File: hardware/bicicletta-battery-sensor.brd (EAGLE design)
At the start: 45.7 x 19.1 mm, 15 parts, among them IC1 LMP92064, IC2 TXB0108

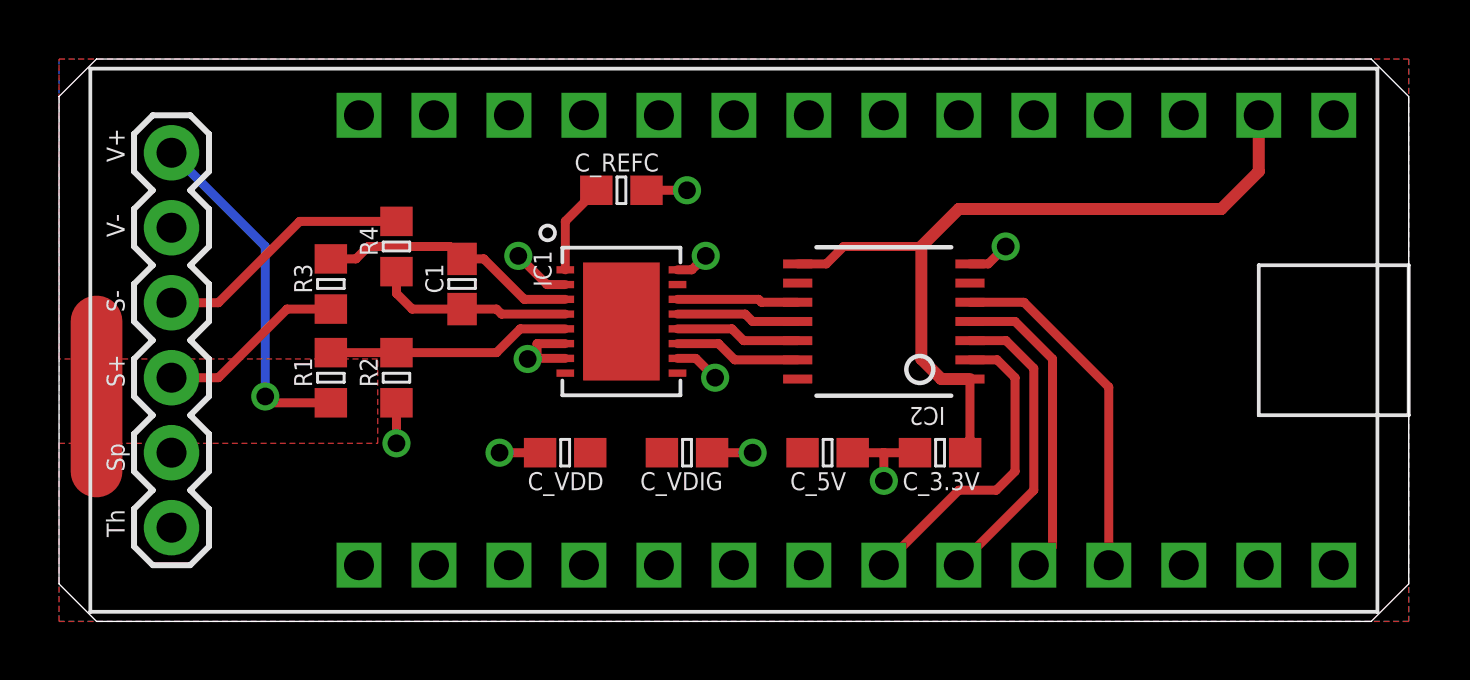
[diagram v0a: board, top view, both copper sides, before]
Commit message: Trying out a new level shifter, as the previous integrated one proved awfully fiddly in practice.
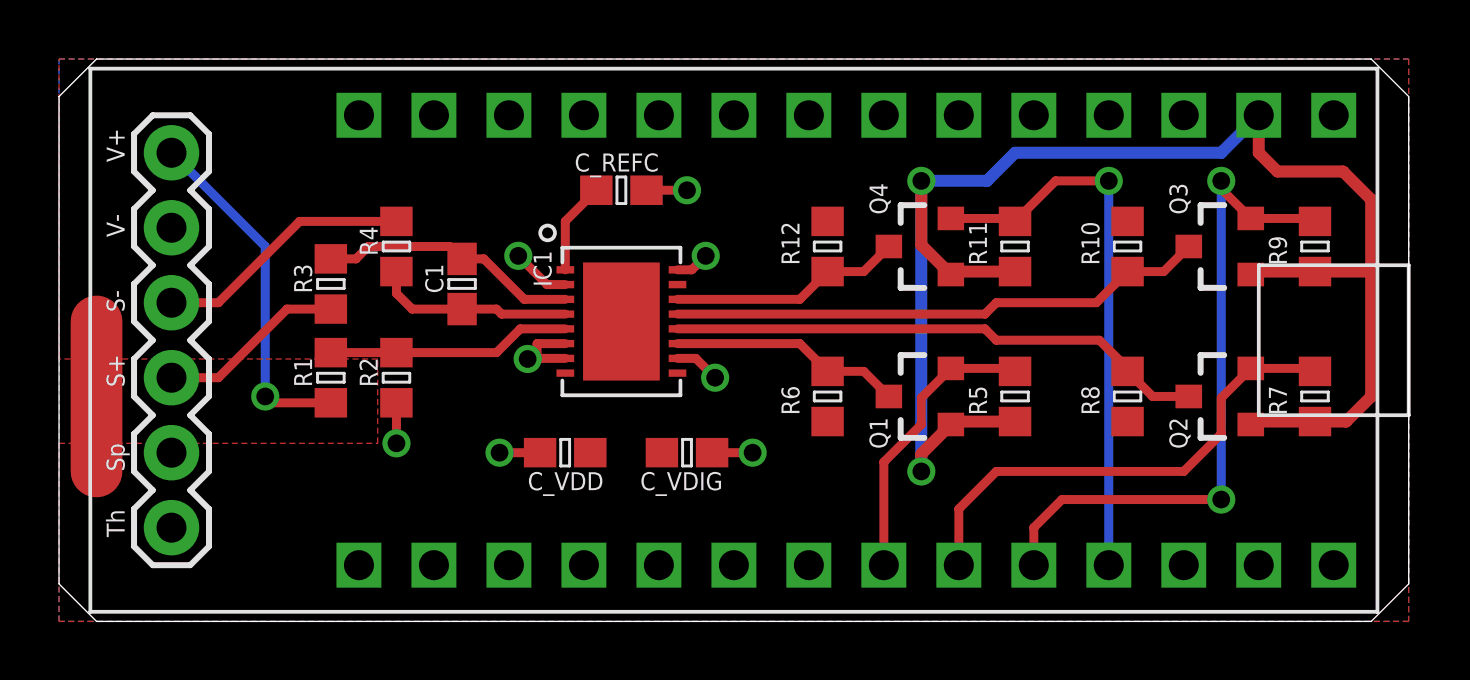
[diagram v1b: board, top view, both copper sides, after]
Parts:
- removed C_3.3V, C_5V: 0.1uF, rcl:C0603
- removed IC2: TXB0108, adafruit:TSSOP14
- added Q1, Q2, Q3, Q4: BSS138, SparkFun-DiscreteSemi:SOT23-3
- added R10, R11, R12, R5, R6, R7, R8, R9: 10K, rcl:R0603
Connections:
- net 3.3V: now also Q1.1, Q2.1, Q3.1, Q4.1, R11.2, R5.2, R7.2, R9.2; no longer C_3.3V.1, IC2.1, IC2.8
- net 5V: now also R10.2, R12.2, R6.2, R8.2; no longer C_5V.1, IC2.14
- net CLK: now also Q3.2, R9.1; no longer IC2.4
- net CLK_5: now also Q3.3, R10.1; no longer IC2.11
- net GND: no longer C_3.3V.2, C_5V.2, IC2.7
- net MISO: now also Q1.2, R5.1; no longer IC2.2
- net MISO_5: now also Q1.3, R6.1; no longer IC2.13
- net MOSI: now also Q2.2, R7.1; no longer IC2.3
- net MOSI_5: now also Q2.3, R8.1; no longer IC2.12
- net SS: now also Q4.2, R11.1; no longer IC2.5
- net SS_5: now also Q4.3, R12.1; no longer IC2.10
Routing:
- net 3.3V: track 27.1 -> 53.2 mm, vias 0 -> 2
- net CLK_5: track 4.18 -> 18.3 mm
- net MOSI_5: track 4.24 -> 18.3 mm
- net CLK: track 10.6 -> 22.7 mm, vias 0 -> 2
- net SS: track 11.9 -> 19.0 mm, vias 0 -> 1
- net MOSI: track 10.3 -> 16.7 mm
- net GND: track 17.9 -> 13.4 mm, vias 10 -> 8
- net SS_5: track 4.11 -> 7.90 mm
- net MISO_5: track 4.30 -> 7.90 mm
- net MISO: track 10.7 -> 9.82 mm

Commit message: Tidying some traces up.
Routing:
- net SS: track 19.0 -> 16.1 mm
- net CLK: track 22.7 -> 21.9 mm
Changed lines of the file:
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@@
 <wire x1="42.445" y1="13.65" x2="42.545" y2="13.55" width="0.3048" layer="1"/>
 <wire x1="33.02" y1="1.905" x2="33.02" y2="3.175" width="0.3048" layer="1"/>
-<wire x1="33.02" y1="3.175" x2="33.9725" y2="4.1275" width="0.3048" layer="1"/>
-<wire x1="33.9725" y1="4.1275" x2="39.37" y2="4.1275" width="0.3048" layer="1"/>
-<via x="39.37" y="4.1275" extent="1-16" drill="0.6"/>
-<wire x1="39.37" y1="4.1275" x2="39.37" y2="14.9225" width="0.3048" layer="16"/>
-<via x="39.37" y="14.9225" extent="1-16" drill="0.6"/>
-<wire x1="40.37" y1="13.65" x2="39.37" y2="14.65" width="0.3048" layer="1"/>
-<wire x1="39.37" y1="14.65" x2="39.37" y2="14.9225" width="0.3048" layer="1"/>
+<wire x1="33.02" y1="3.175" x2="34.29" y2="4.445" width="0.3048" layer="1"/>
+<wire x1="34.29" y1="4.445" x2="39.37" y2="4.445" width="0.3048" layer="1"/>
+<via x="39.37" y="4.445" extent="1-16" drill="0.6"/>
+<via x="39.37" y="14.605" extent="1-16" drill="0.6"/>
+<wire x1="40.37" y1="13.65" x2="39.415" y2="14.605" width="0.3048" layer="1"/>
+<wire x1="39.415" y1="14.605" x2="39.37" y2="14.605" width="0.3048" layer="1"/>
+<wire x1="39.37" y1="14.605" x2="39.37" y2="4.445" width="0.3048" layer="16"/>
 </signal>
 <signal name="SS">
@@
 <contactref element="Q4" pad="2"/>
 <contactref element="R11" pad="1"/>
-<wire x1="35.56" y1="1.905" x2="35.56" y2="14.9225" width="0.3048" layer="16"/>
-<via x="35.56" y="14.9225" extent="1-16" drill="0.6"/>
-<wire x1="35.56" y1="14.9225" x2="33.7575" y2="14.9225" width="0.3048" layer="1"/>
-<wire x1="33.7575" y1="14.9225" x2="32.385" y2="13.55" width="0.3048" layer="1"/>
+<via x="33.655" y="13.6525" extent="1-16" drill="0.6"/>
 <wire x1="30.21" y1="13.65" x2="32.285" y2="13.65" width="0.3048" layer="1"/>
 <wire x1="32.285" y1="13.65" x2="32.385" y2="13.55" width="0.3048" layer="1"/>
+<wire x1="32.385" y1="13.55" x2="32.4875" y2="13.6525" width="0.3048" layer="1"/>
+<wire x1="32.4875" y1="13.6525" x2="33.655" y2="13.6525" width="0.3048" layer="1"/>
+<wire x1="33.655" y1="13.6525" x2="35.56" y2="11.7475" width="0.3048" layer="16"/>
+<wire x1="35.56" y1="11.7475" x2="35.56" y2="1.905" width="0.3048" layer="16"/>
 </signal>
 <signal name="~D9/A9">
@@
 <wire x1="29.21" y1="5.08" x2="29.21" y2="14.9225" width="0.4064" layer="16"/>
 <via x="29.21" y="14.9225" extent="1-16" drill="0.6"/>
-<wire x1="31.4325" y1="14.9225" x2="32.385" y2="15.875" width="0.4064" layer="16"/>
-<wire x1="32.385" y1="15.875" x2="39.37" y2="15.875" width="0.4064" layer="16"/>
+<wire x1="29.21" y1="14.9225" x2="30.1625" y2="15.875" width="0.4064" layer="16"/>
+<wire x1="30.1625" y1="15.875" x2="39.37" y2="15.875" width="0.4064" layer="16"/>
 <wire x1="39.37" y1="15.875" x2="40.64" y2="17.145" width="0.4064" layer="16"/>
-<wire x1="31.4325" y1="14.9225" x2="29.21" y2="14.9225" width="0.4064" layer="16"/>
 <wire x1="30.21" y1="6.67" x2="29.21" y2="5.67" width="0.4064" layer="1"/>
 <wire x1="29.21" y1="5.67" x2="29.21" y2="5.08" width="0.4064" layer="1"/>
@@
 </signal>
 </signals>
+<errors>
+</errors>
 </board>
 </drawing>
